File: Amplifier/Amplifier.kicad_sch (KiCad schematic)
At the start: 27 parts, among them U1 SKY65111-348LF, U2 MAX2633EUT+T, U3 RLM-23-1WL+

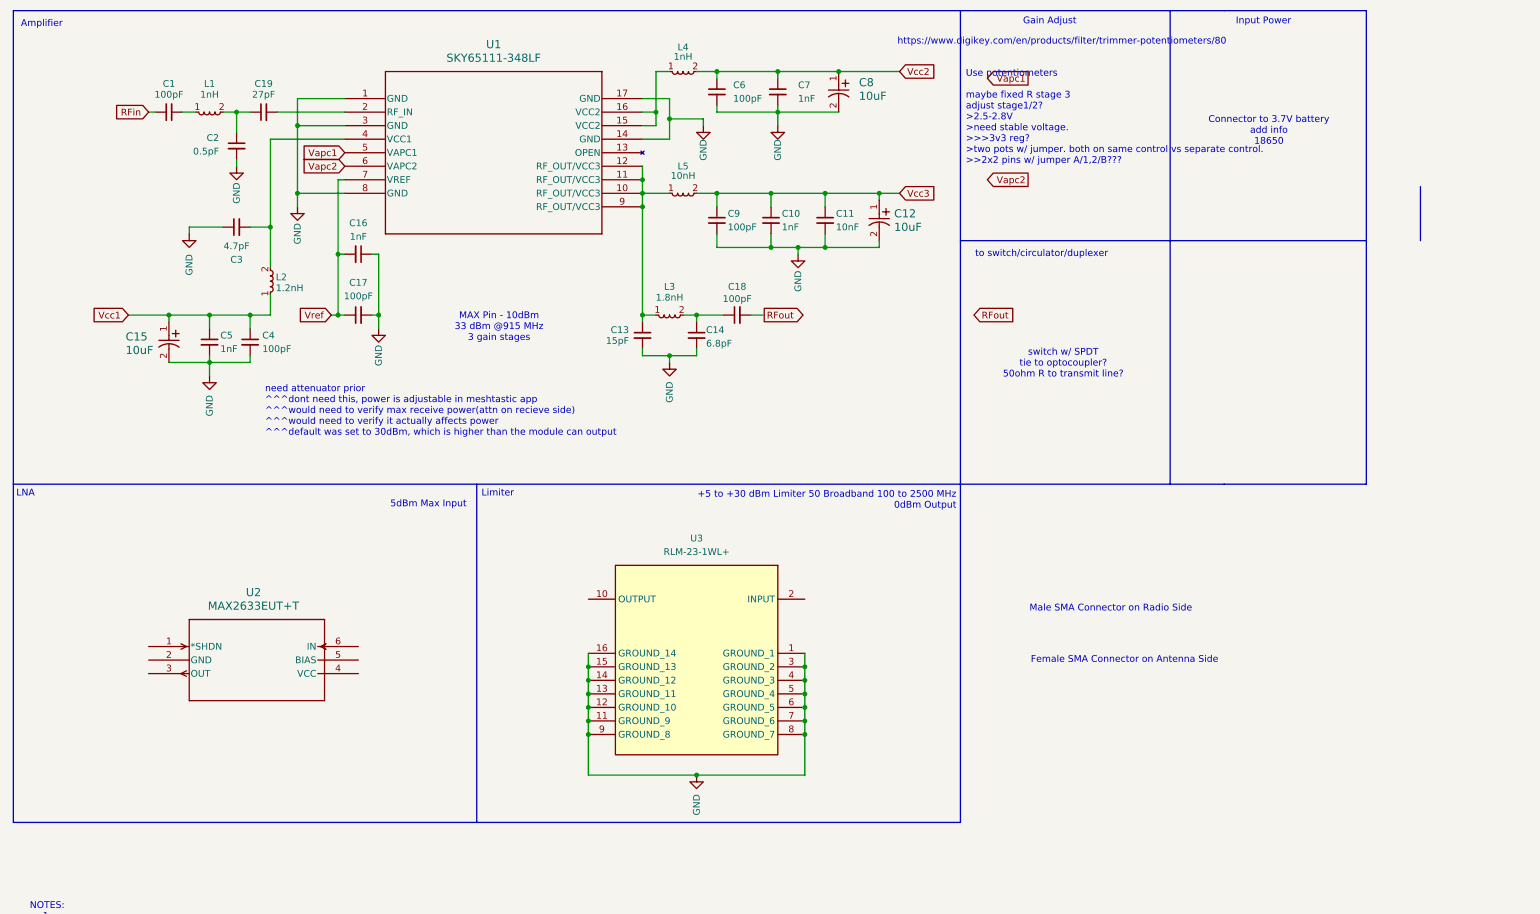
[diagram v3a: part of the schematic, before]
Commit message: updatred schematic. added Male/Female SMA connectors.
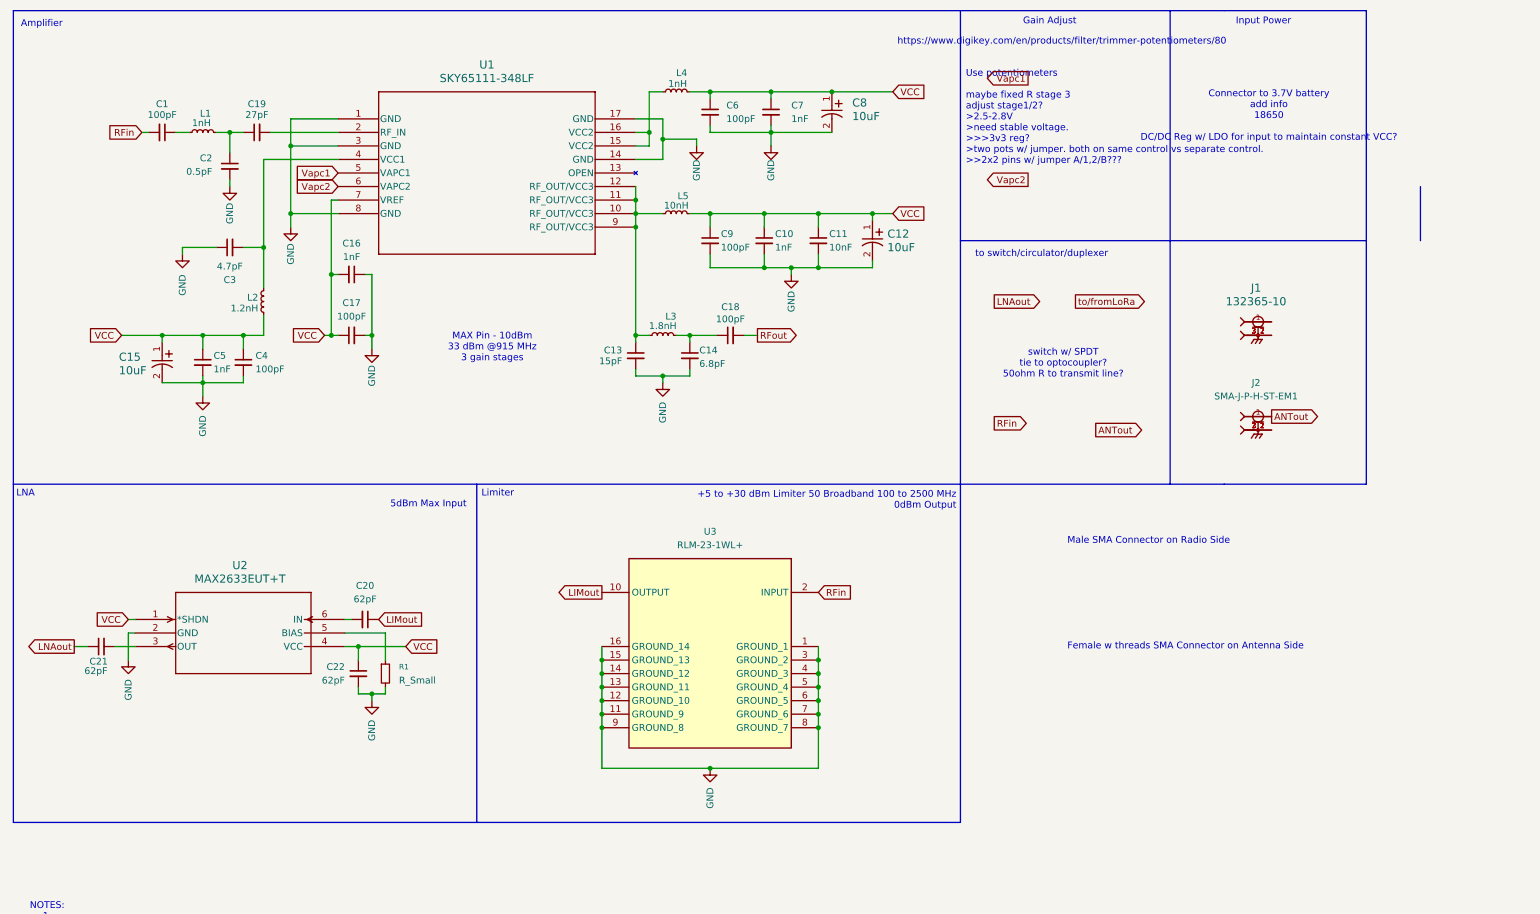
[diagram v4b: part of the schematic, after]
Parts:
- added C20, C21, C22: 62pF, Capacitor_SMD:C_0603_1608Metric, symbol amp:62pF
- added J1: 132365-10, amp:CONN_132365-10_AMP, symbol amp:132365-10
- added J2: SMA-J-P-H-ST-EM1, amp:SAMTEC_SMA-J-P-H-ST-EM1, symbol amp:SMA-J-P-H-ST-EM1
- added R1: R_Small, symbol Device:R_Small
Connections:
- net Vcc1 is gone; now on net VCC: C15.1, C4.1, C5.1, L2.1
- net Vcc2 is gone; now on net VCC: C6.1, C7.1, C8.1, L4.2
- net Vcc3 is gone; now on net VCC: C10.1, C11.1, C12.1, C9.1, L5.2
- net Vref is gone; now on net VCC: C16.2, C17.1, U1.7 (VREF)
- net GND: now also U2.2 (GND), C22.2, R1.2
- net RFin: now also U3.2 (INPUT)
- net VCC: now reaches U2.1 (*SHDN)
- net VCC: now also U2.4 (VCC), C22.1
- net at U2.3 (OUT): now also C21.2
- net at U2.5 (BIAS): now also R1.1
- net at U2.6 (IN): now also C20.2
- net LIMout: now reaches U3.10 (OUTPUT)
- net LIMout: now also C20.1
- new net: J2.2_1, J2.2_2, J2.3_1, J2.3_2
- new net: J1.2_2, J1.3_1, J1.3_2
- new net ANTout: J2.1
- new net LNAout: C21.1
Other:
- note added: "Connector to 3.7V battery add info 18650 DC/DC Reg w/ LDO for input to maintain constant VCC?"
- note added: "Female w threads SMA Connector on Antenna Side"
- note removed: "Connector to 3.7V battery add info 18650"
- note removed: "Female SMA Connector on Antenna Side"
- note removed: "need attenuator prior ^^^dont need this, power is adjustable in meshtastic app ^^^would need to verify max receive power(attn on recieve side) ^^^would need to verify it actually affects power ^^^default was set to 30dBm, which is higher than the module can output"
- moved on the sheet: C1, C10, C11, C12, C13, C14, C15, C16, C17, C18, C19, C2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

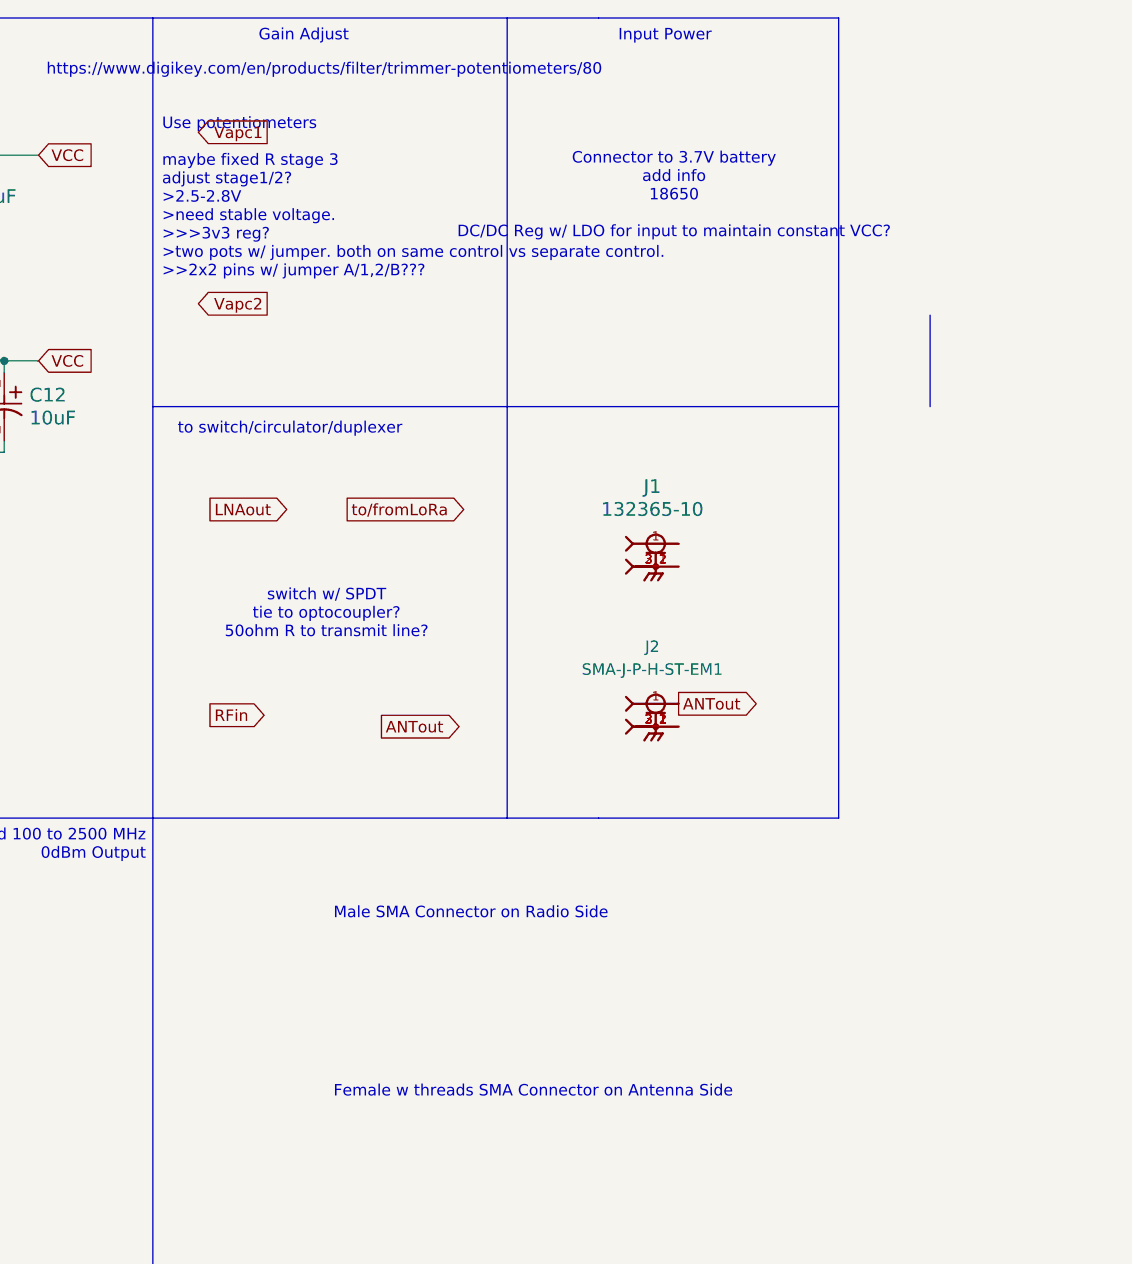
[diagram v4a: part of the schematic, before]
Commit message: updated schematic layout and notes. added SMA connectors
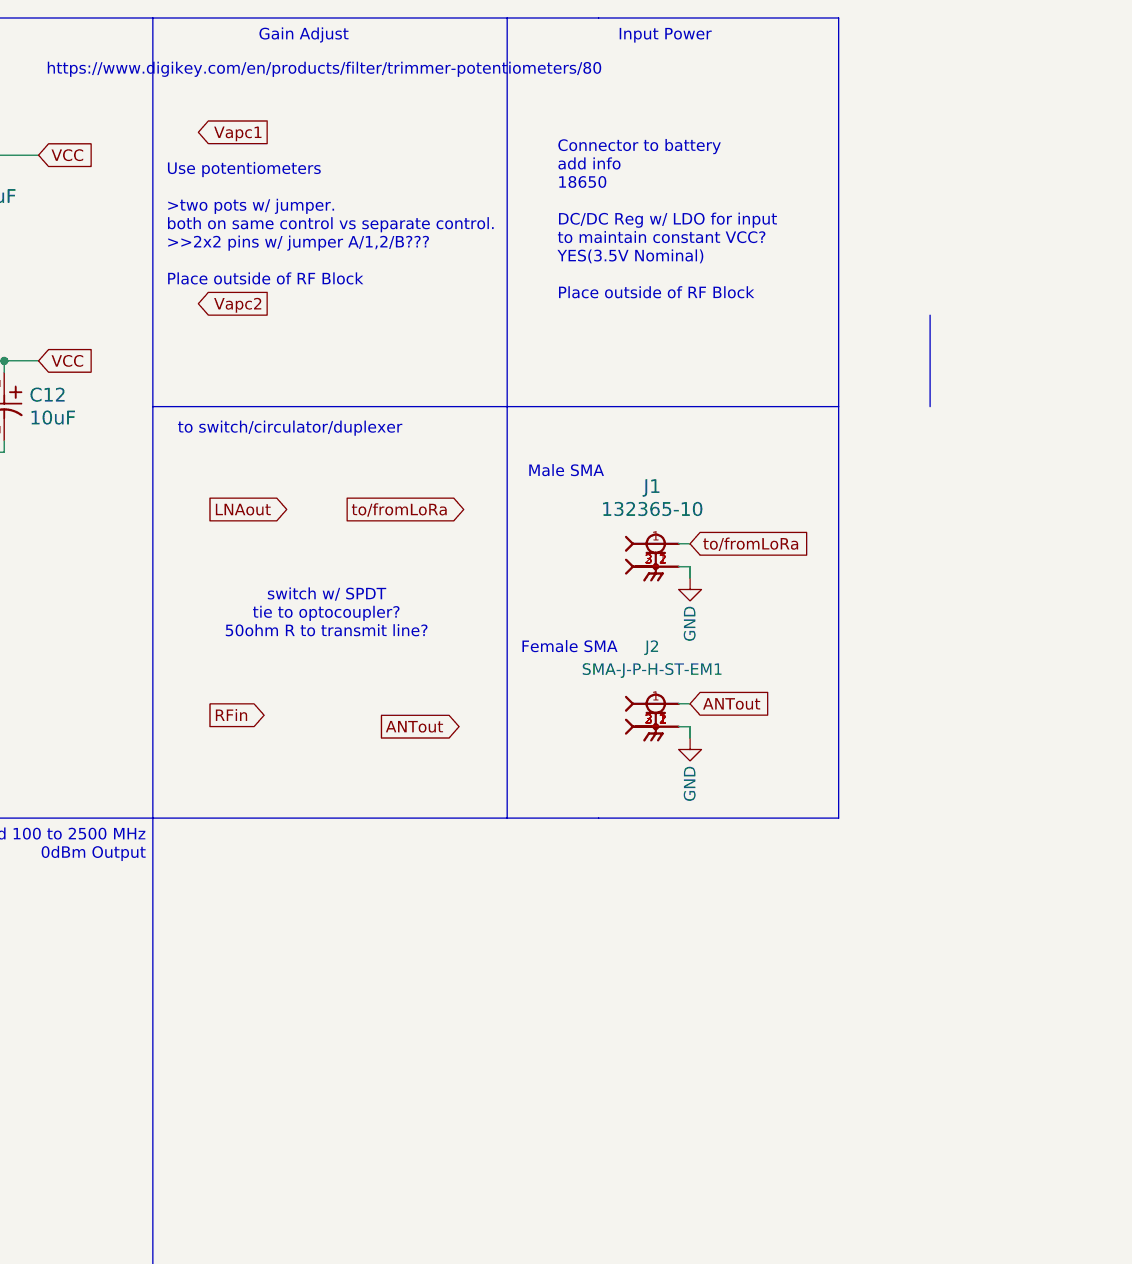
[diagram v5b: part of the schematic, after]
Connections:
- net GND: now also J1.2_2, J1.3_1, J1.3_2, J2.2_1, J2.2_2, J2.3_1, J2.3_2
- net to/fromLoRa: now also J1.1
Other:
- note added: "Connector to battery add info 18650 DC/DC Reg w/ LDO for input to maintain constant VCC? YES(3.5V Nominal) Place outside of RF Block"
- note added: "Female SMA"
- note added: "Male SMA"
- note added: "Use potentiometers >two pots w/ jumper. both on same control vs separate control. >>2x2 pins w/ jumper A/1,2/B??? Place outside of RF Block"
- note removed: "Connector to 3.7V battery add info 18650 DC/DC Reg w/ LDO for input to maintain constant VCC?"
- note removed: "Female w threads SMA Connector on Antenna Side"
- note removed: "Male SMA Connector on Radio Side"
- note removed: "Use potentiometers maybe fixed R stage 3 adjust stage1/2? >2.5-2.8V >need stable voltage. >>>3v3 reg? >two pots w/ jumper. both on same control vs separate control. >>2x2 pins w/ jumper A/1,2/B???"

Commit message: added pots for voltage select
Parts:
- added R2, R3: 1k, symbol Device:R
- added VR1, VR2: 3386G-1-102LF, amp:POT_3386G, symbol amp:3386G-1-102LF
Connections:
- net VCC: now also R2.1, R3.1
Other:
- note added: "Gain Adjust - Stage 1/2"
- note added: "Gain Adjust - Stage 3"
- note added: "NOTES: 1. 2. 3. 4. Pretend I didn't work out of main"
- note added: "Set this"
- note added: "https://www.digikey.com/en/products/detail/bourns-inc/3386P-1-472LF/2537240"
- note removed: "Gain Adjust"
- note removed: "NOTES: 1. 2. 3. 4."
- note removed: "Use potentiometers >two pots w/ jumper. both on same control vs separate control. >>2x2 pins w/ jumper A/1,2/B??? Place outside of RF Block"
- note removed: "https://www.digikey.com/en/products/filter/trimmer-potentiometers/80"

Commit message: aded switches and 3v3 regulator. updated schematic. removed notes/support
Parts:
- added U4, U5: SKYA21001, amp:SOT65P220X110-6N, symbol amp:SKYA21001
- added U6: TPS61221DCKR, amp:DCK0006A, symbol amp:TPS61221DCKR
- R2, R3: value 1k -> 800
- VR1, VR2: value 3386G-1-102LF -> 4.7k
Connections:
- net GND: now also VR1.1, VR2.1, U4.2 (GND), U5.2 (GND)
- net LNAout: now also U4.1 (J3)
- net RFin: now also U4.3 (J2); no longer U3.2 (INPUT)
- net RFout: now also U5.1 (J3)
- net VCC: no longer R2.1, R3.1
- net Vapc1: now also R2.2, VR1.2
- net Vapc2: now also R3.2, VR2.2
- net ANTout renamed ANT
- net ANT: now also U5.5 (J1)
- net to/fromLoRa renamed LoRa
- net LoRa: now also U4.5 (J1)
- new net 3v3: R2.1, R3.1
- new net INPUT: U3.2 (INPUT), U5.3 (J2)
- no-connect marks 0 -> 2
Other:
- note added: "Connector to battery add info 18650 DC/DC Reg a 3.3/3.5 JUST FOR GAIN ADJUST Place outside of RF Block"
- note removed: "Connector to battery add info 18650 DC/DC Reg w/ LDO for input to maintain constant VCC? YES(3.5V Nominal) Place outside of RF Block"
- note removed: "DONT NEED PHASE SHIFTER BC THAT IS HANDLED BY LILYGO TRANSCEIVER CIRCUIT"
- note removed: "https://www.digikey.com/en/products/detail/bourns-inc/3386P-1-472LF/2537240"
- note removed: "switch w/ SPDT tie to optocoupler? 50ohm R to transmit line?"
- note removed: "~250mW output power max allowable output power 30dBm/1W(federally regulated) 22dBm outputs lilygo unit https://wiki.lilygo.cc/products/t-beam-series/t-beam-supreme/"
- moved on the sheet: R2, R3
